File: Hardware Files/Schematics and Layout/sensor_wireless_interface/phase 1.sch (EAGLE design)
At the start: 5 parts, among them U1 RHD2216

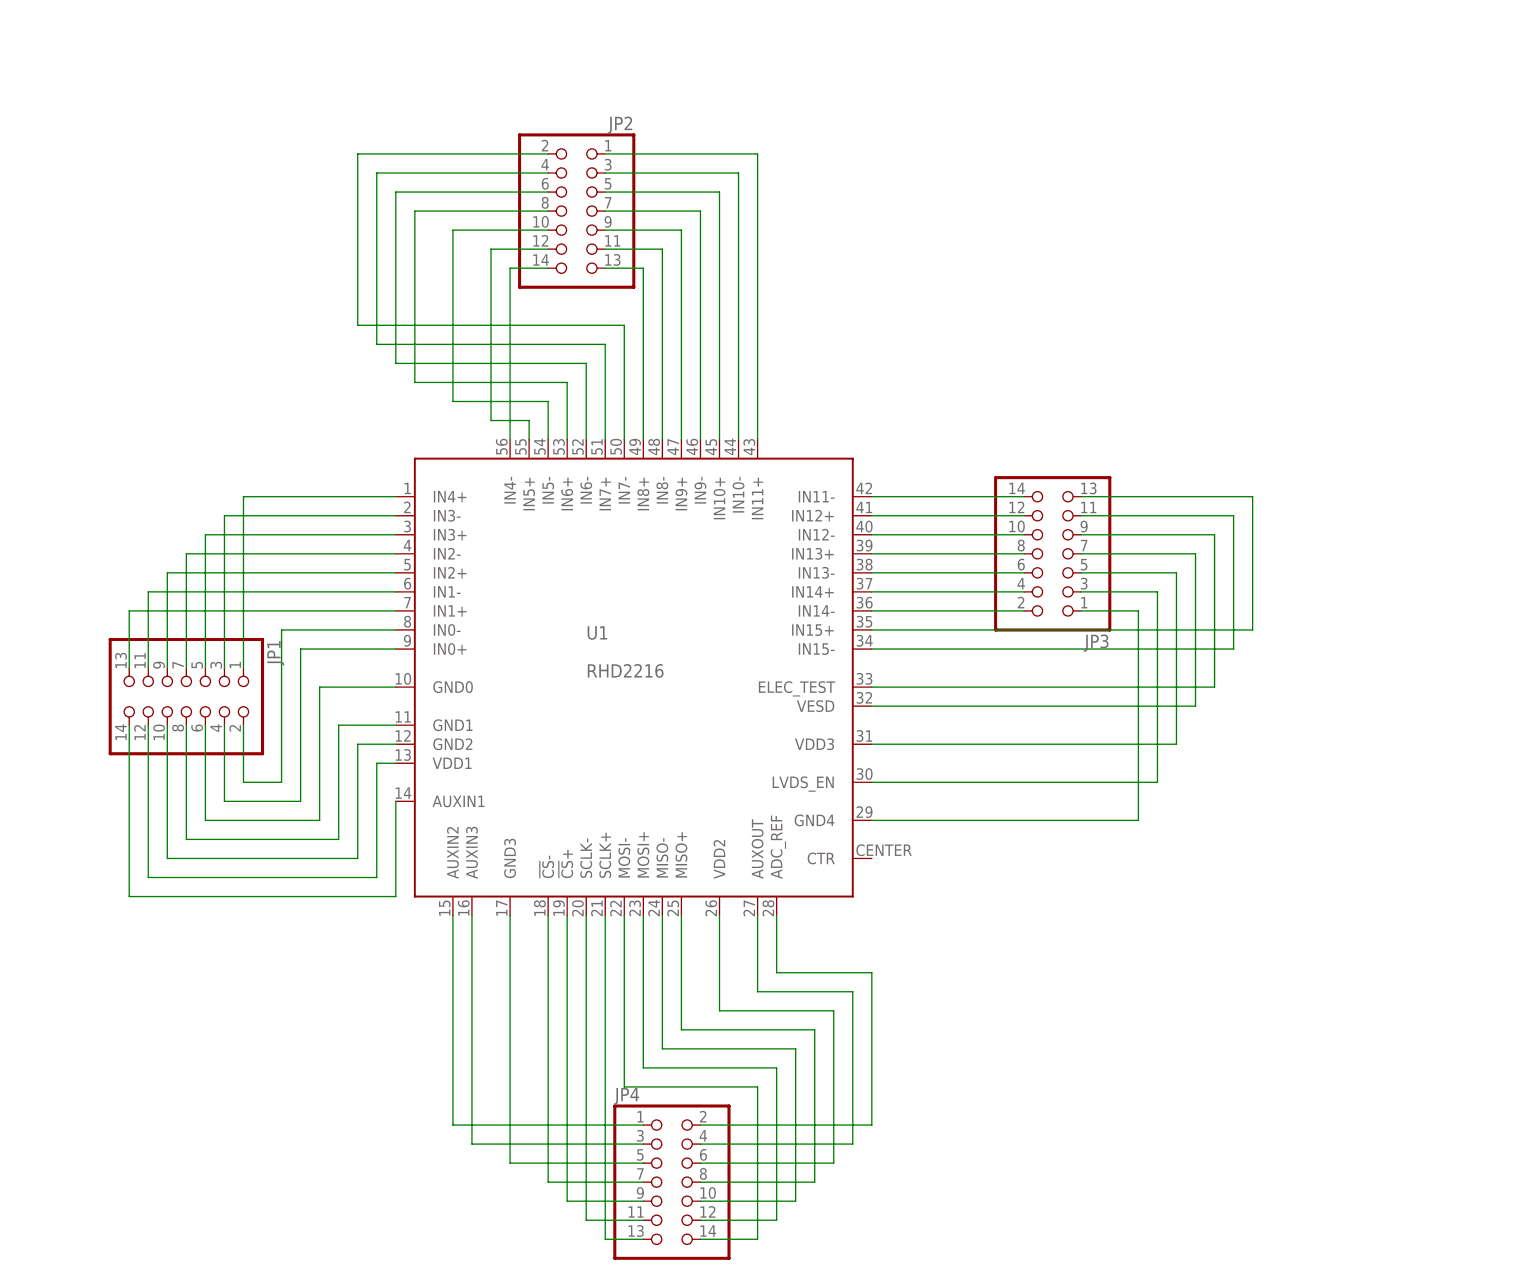
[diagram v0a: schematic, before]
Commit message: updated pin assignment for better routing
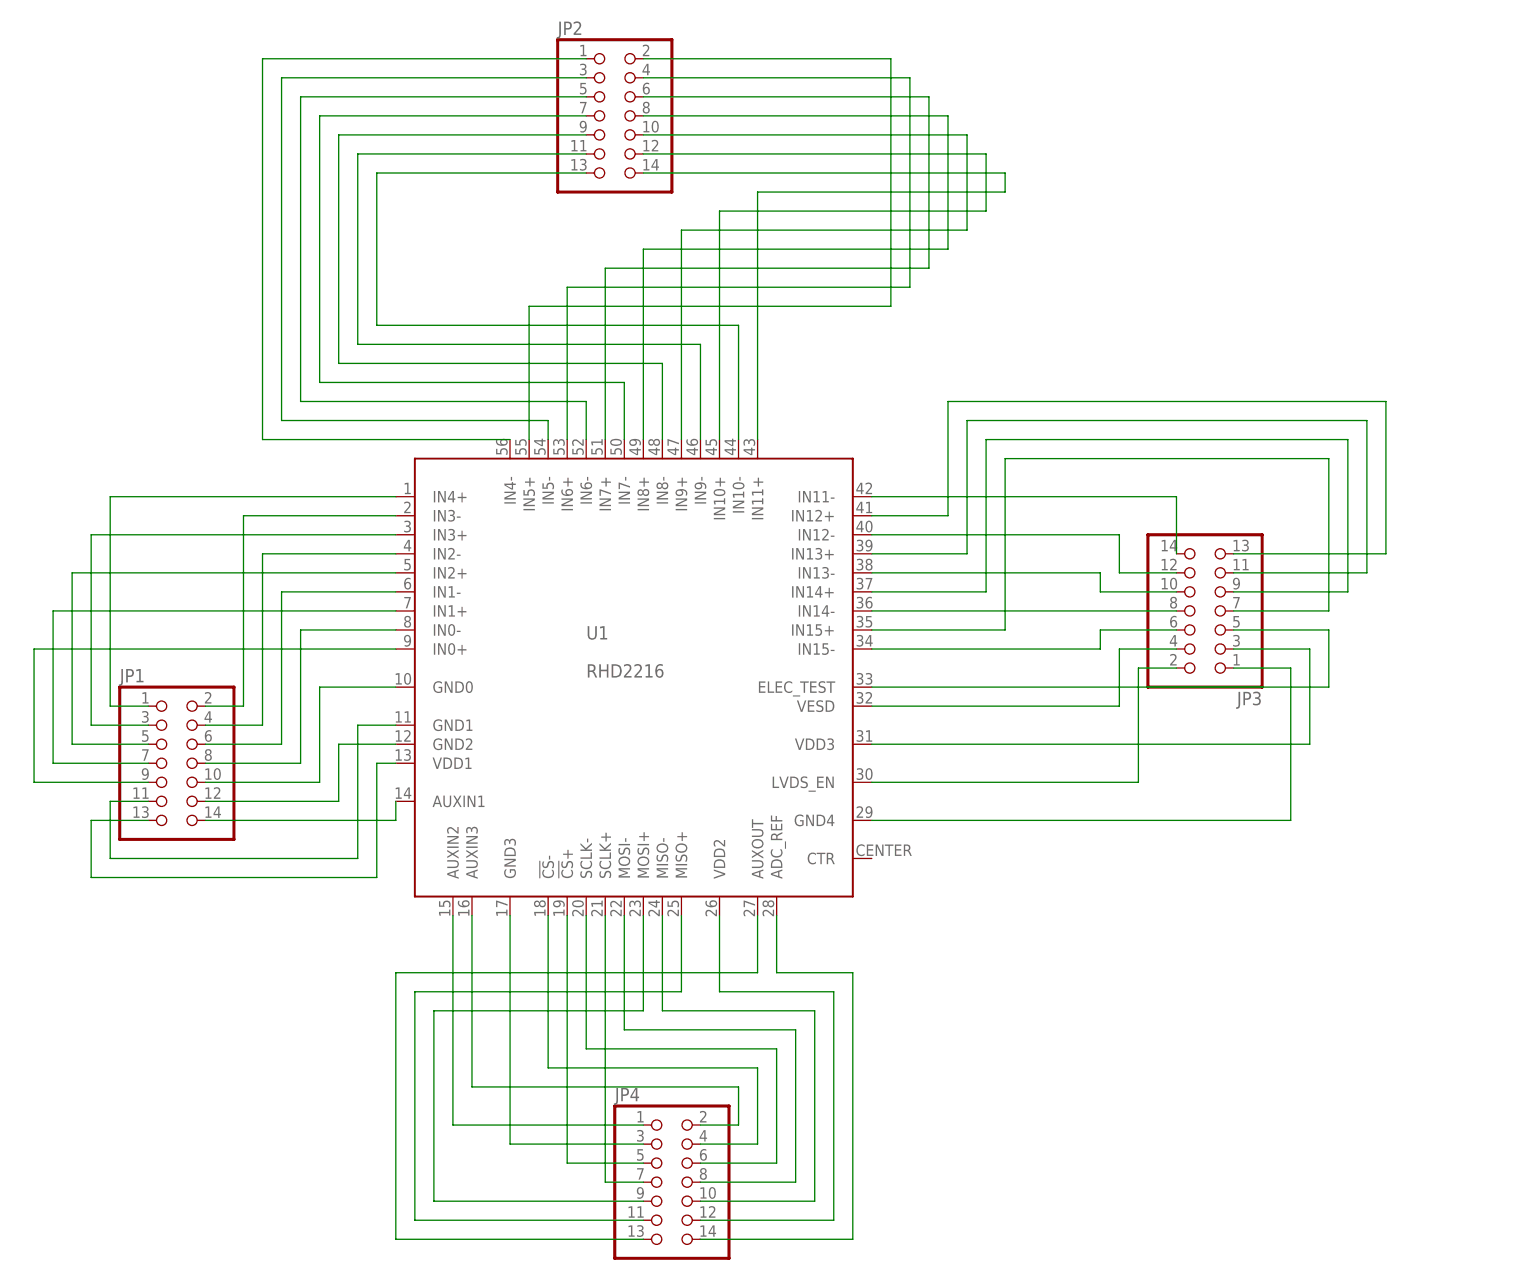
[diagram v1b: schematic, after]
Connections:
- removed net N$12 (its old number): JP1.10, U1.GND2
- removed net N$2 (its old number): JP1.3, U1.IN3-
- removed net N$56 (its old number): JP3.2, U1.IN14-
- new net N$1: JP1.12, U1.GND2
- new net N$14: JP1.13, U1.VDD1
- new net N$50: JP3.2, U1.LVDS_EN
- net N$10: now also JP1.8, U1.IN0-; no longer JP1.6, U1.GND0
- net N$11: now also JP1.10, U1.GND0; no longer JP1.8, U1.GND1
- net N$13: now also JP1.11, U1.GND1; no longer JP1.12, U1.VDD1
- net N$15: now also U1.IN4-; no longer U1.IN11+
- net N$16: now also U1.IN5-; no longer U1.IN10-
- net N$17: now also U1.IN6-; no longer U1.IN10+
- net N$19: now also U1.IN7-; no longer U1.IN9-
- net N$20: now also U1.IN8-; no longer U1.IN9+
- net N$21: now also U1.IN9-; no longer U1.IN8-
- net N$22: now also U1.IN10-; no longer U1.IN8+
- net N$23: now also JP2.2, U1.IN5+; no longer JP2.14, U1.IN4-
- net N$24: now also JP2.4, U1.IN6+; no longer JP2.12, U1.IN5+
- net N$25: now also JP2.6, U1.IN7+; no longer JP2.10, U1.IN5-
- net N$26: now also U1.IN8+; no longer U1.IN6+
- net N$27: now also JP2.10, U1.IN9+; no longer JP2.6, U1.IN6-
- net N$28: now also JP2.12, U1.IN10+; no longer JP2.4, U1.IN7+
- net N$29: now also JP2.14, U1.IN11+; no longer JP2.2, U1.IN7-
- net N$3: now also JP1.2, U1.IN3-; no longer JP1.5, U1.IN3+
- net N$30: now also JP4.2; no longer JP4.3
- net N$31: now also JP4.3; no longer JP4.5
- net N$32: now also JP4.4; no longer JP4.7
- net N$33: now also JP4.5; no longer JP4.9
- net N$34: now also JP4.6; no longer JP4.11
- net N$35: now also JP4.7; no longer JP4.13
- net N$36: now also JP4.8; no longer JP4.14
- net N$37: now also JP4.9; no longer JP4.12
- net N$39: now also JP4.11; no longer JP4.8
- net N$4: now also JP1.3, U1.IN3+; no longer JP1.7, U1.IN2-
- net N$40: now also JP4.12; no longer JP4.6
- net N$41: now also JP4.13; no longer JP4.4
- net N$42: now also JP4.14; no longer JP4.2
- net N$44: now also U1.VDD3; no longer U1.LVDS_EN
- net N$45: now also U1.ELEC_TEST; no longer U1.VDD3
- net N$46: now also U1.IN15+; no longer U1.VESD
- net N$47: now also U1.IN14+; no longer U1.ELEC_TEST
- net N$48: now also U1.IN13+; no longer U1.IN15-
- net N$49: now also U1.IN12+; no longer U1.IN15+
- net N$5: now also JP1.5; no longer JP1.9
- net N$51: now also JP3.4, U1.VESD; no longer JP3.12, U1.IN12+
- net N$52: now also JP3.6, U1.IN15-; no longer JP3.10, U1.IN12-
- net N$53: now also U1.IN14-; no longer U1.IN13+
- net N$54: now also JP3.10; no longer JP3.6
- net N$55: now also JP3.12, U1.IN12-; no longer JP3.4, U1.IN14+
- net N$6: now also JP1.7, U1.IN1+; no longer JP1.11, U1.IN1-
- net N$7: now also JP1.9, U1.IN0+; no longer JP1.13, U1.IN1+
- net N$8: now also JP1.4, U1.IN2-; no longer JP1.2, U1.IN0-
- net N$9: now also JP1.6, U1.IN1-; no longer JP1.4, U1.IN0+
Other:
- moved on the sheet: JP1, JP2, JP3

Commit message: changed to more specific schematic
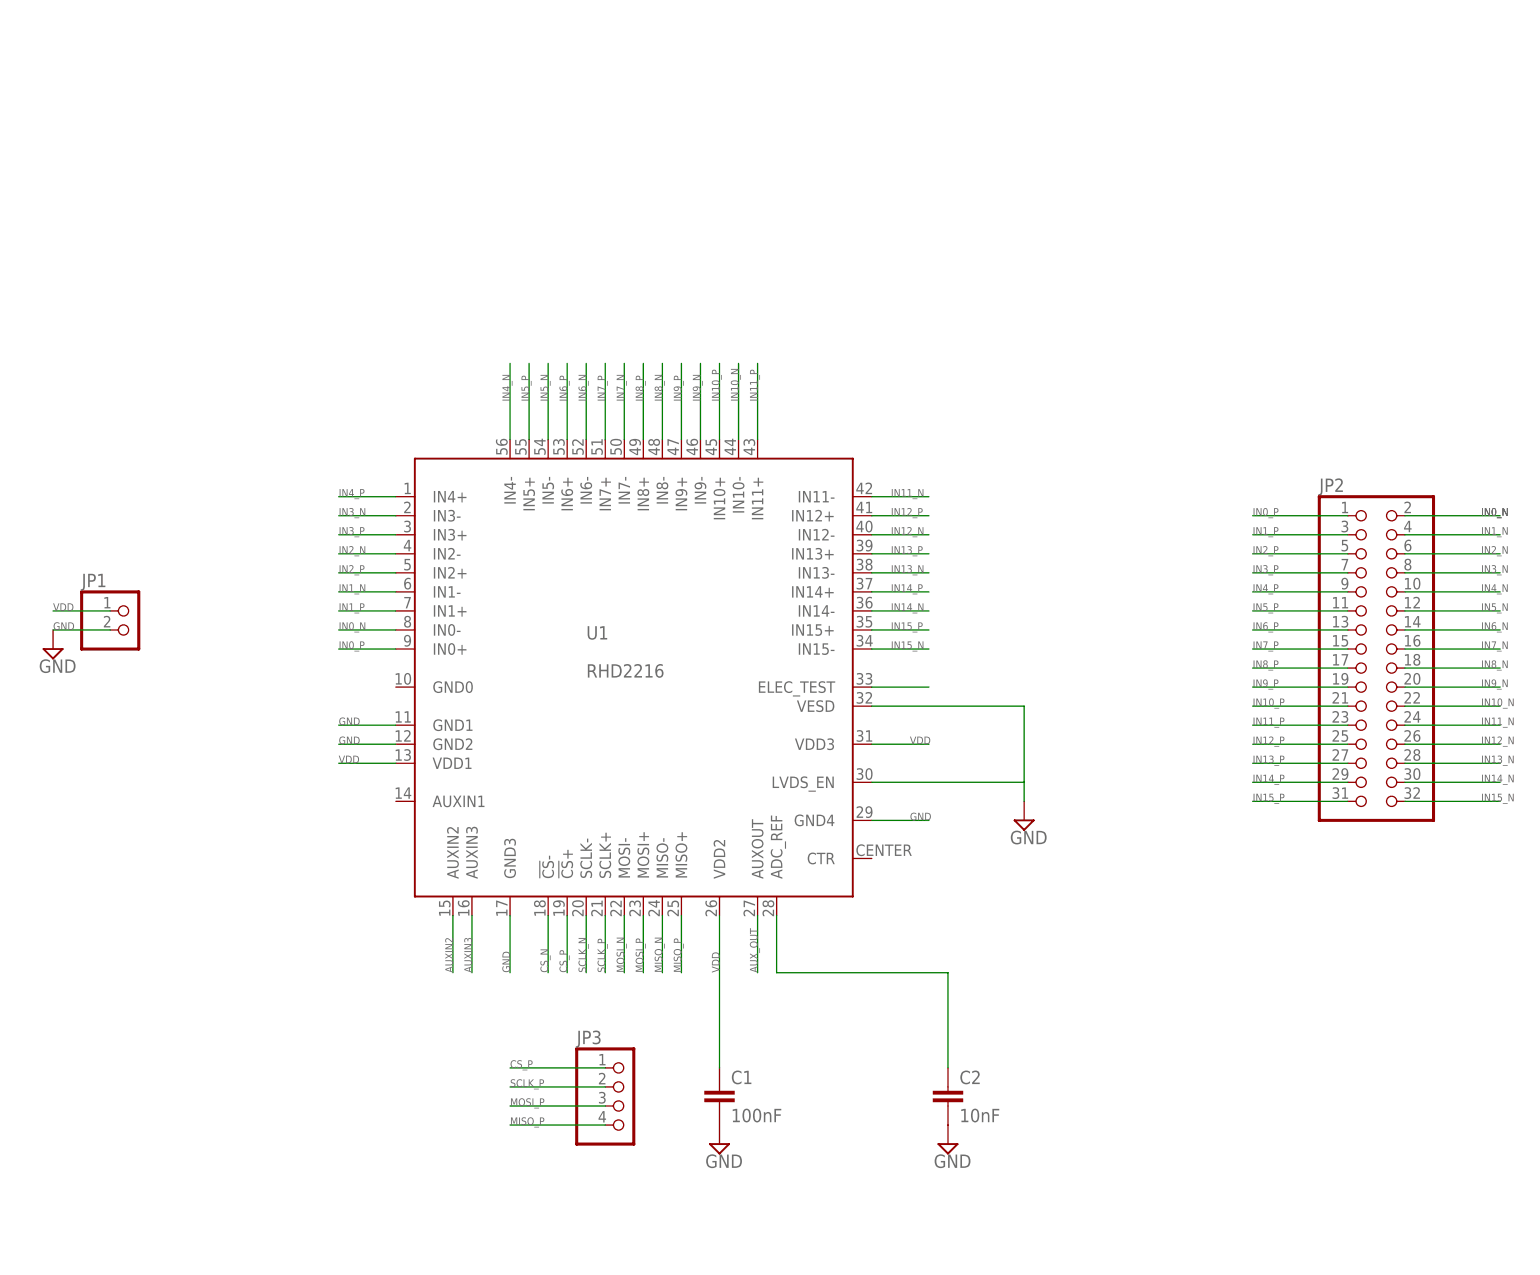
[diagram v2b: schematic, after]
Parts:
- removed JP4: (no value), pinhead:PINHD-2X7
- added C1: 100nF, capacitor-wima:C2.5/2
- added C2: 10nF, capacitor-wima:C2.5/2
- JP1: device pinhead:PINHD-2X7 -> pinhead:PINHD-1X2
- JP2: device pinhead:PINHD-2X7 -> pinhead:PINHD-2X16
- JP3: device pinhead:PINHD-2X7 -> pinhead:PINHD-1X4
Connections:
- removed net N$11: JP1.10, U1.GND0
- removed net N$12: JP1.14, U1.AUXIN1
- removed net N$13: JP1.11, U1.GND1
- removed net N$14: JP1.13, U1.VDD1
- removed net N$15: JP2.1, U1.IN4-
- removed net N$16: JP2.3, U1.IN5-
- removed net N$17: JP2.5, U1.IN6-
- removed net N$18: JP4.1, U1.AUXIN2
- removed net N$19: JP2.7, U1.IN7-
- removed net N$2: JP1.1, U1.IN4+
- removed net N$20: JP2.9, U1.IN8-
- removed net N$21: JP2.11, U1.IN9-
- removed net N$22: JP2.13, U1.IN10-
- removed net N$23: JP2.2, U1.IN5+
- removed net N$24: JP2.4, U1.IN6+
- removed net N$25: JP2.6, U1.IN7+
- removed net N$26: JP2.8, U1.IN8+
- removed net N$27: JP2.10, U1.IN9+
- removed net N$28: JP2.12, U1.IN10+
- removed net N$29: JP2.14, U1.IN11+
- removed net N$3: JP1.2, U1.IN3-
- removed net N$30: JP4.2, U1.AUXIN3
- removed net N$31: JP4.3, U1.GND3
- removed net N$32: JP4.4, U1.!CS!-
- removed net N$33: JP4.5, U1.!CS!+
- removed net N$34: JP4.6, U1.SCLK-
- removed net N$35: JP4.7, U1.SCLK+
- removed net N$36: JP4.8, U1.MOSI-
- removed net N$37: JP4.9, U1.MOSI+
- removed net N$38: JP4.10, U1.MISO-
- removed net N$39: JP4.11, U1.MISO+
- removed net N$4: JP1.3, U1.IN3+
- removed net N$40: JP4.12, U1.VDD2
- removed net N$41: JP4.13, U1.AUXOUT
- removed net N$42: JP4.14, U1.ADC_REF
- removed net N$43: JP3.1, U1.GND4
- removed net N$44: JP3.3, U1.VDD3
- removed net N$45: JP3.5, U1.ELEC_TEST
- removed net N$46: JP3.7, U1.IN15+
- removed net N$47: JP3.9, U1.IN14+
- removed net N$48: JP3.11, U1.IN13+
- removed net N$49: JP3.13, U1.IN12+
- removed net N$5: JP1.5, U1.IN2+
- removed net N$50: JP3.2, U1.LVDS_EN
- removed net N$51: JP3.4, U1.VESD
- removed net N$52: JP3.6, U1.IN15-
- removed net N$53: JP3.8, U1.IN14-
- removed net N$54: JP3.10, U1.IN13-
- removed net N$55: JP3.12, U1.IN12-
- removed net N$56: JP3.14, U1.IN11-
- removed net N$6: JP1.7, U1.IN1+
- removed net N$7: JP1.9, U1.IN0+
- removed net N$8: JP1.4, U1.IN2-
- removed net N$9: JP1.6, U1.IN1-
- new net AUXIN2: U1.AUXIN2
- new net AUXIN3: U1.AUXIN3
- new net AUX_OUT: U1.AUXOUT
- new net CS_N: U1.!CS!-
- new net CS_P: JP3.1, U1.!CS!+
- new net GND: C1.2, C2.2, JP1.2, U1.GND1, U1.GND2, U1.GND3, U1.GND4, U1.LVDS_EN, U1.VESD
- new net IN0_N: JP2.2, U1.IN0-
- new net IN0_P: JP2.1, U1.IN0+
- new net IN10_N: JP2.22, U1.IN10-
- new net IN10_P: JP2.21, U1.IN10+
- new net IN11_N: JP2.24, U1.IN11-
- new net IN11_P: JP2.23, U1.IN11+
- new net IN12_N: JP2.26, U1.IN12-
- new net IN12_P: JP2.25, U1.IN12+
- new net IN13_N: JP2.28, U1.IN13-
- new net IN13_P: JP2.27, U1.IN13+
- new net IN14_N: JP2.30, U1.IN14-
- new net IN14_P: JP2.29, U1.IN14+
- new net IN15_N: JP2.32, U1.IN15-
- new net IN15_P: JP2.31, U1.IN15+
- new net IN1_N: JP2.4, U1.IN1-
- new net IN1_P: JP2.3, U1.IN1+
- new net IN2_N: JP2.6, U1.IN2-
- new net IN2_P: JP2.5, U1.IN2+
- new net IN3_N: JP2.8, U1.IN3-
- new net IN3_P: JP2.7, U1.IN3+
- new net IN4_N: JP2.10, U1.IN4-
- new net IN4_P: JP2.9, U1.IN4+
- new net IN5_N: JP2.12, U1.IN5-
- new net IN5_P: JP2.11, U1.IN5+
- new net IN6_N: JP2.14, U1.IN6-
- new net IN6_P: JP2.13, U1.IN6+
- new net IN7_N: JP2.16, U1.IN7-
- new net IN7_P: JP2.15, U1.IN7+
- new net IN8_N: JP2.18, U1.IN8-
- new net IN8_P: JP2.17, U1.IN8+
- new net IN9_N: JP2.20, U1.IN9-
- new net IN9_P: JP2.19, U1.IN9+
- new net MISO_N: U1.MISO-
- new net MISO_P: JP3.4, U1.MISO+
- new net MOSI_N: U1.MOSI-
- new net MOSI_P: JP3.3, U1.MOSI+
- new net SCLK_N: U1.SCLK-
- new net SCLK_P: JP3.2, U1.SCLK+
- new net VDD: C1.1, JP1.1, U1.VDD1, U1.VDD2, U1.VDD3
- net N$1: now also C2.1, U1.ADC_REF; no longer JP1.12, U1.GND2
- net N$10: now also U1.ELEC_TEST; no longer JP1.8, U1.IN0-
